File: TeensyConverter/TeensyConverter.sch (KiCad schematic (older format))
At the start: 5 parts, among them P1 CONN_01X03, U1 Teensy-3.2

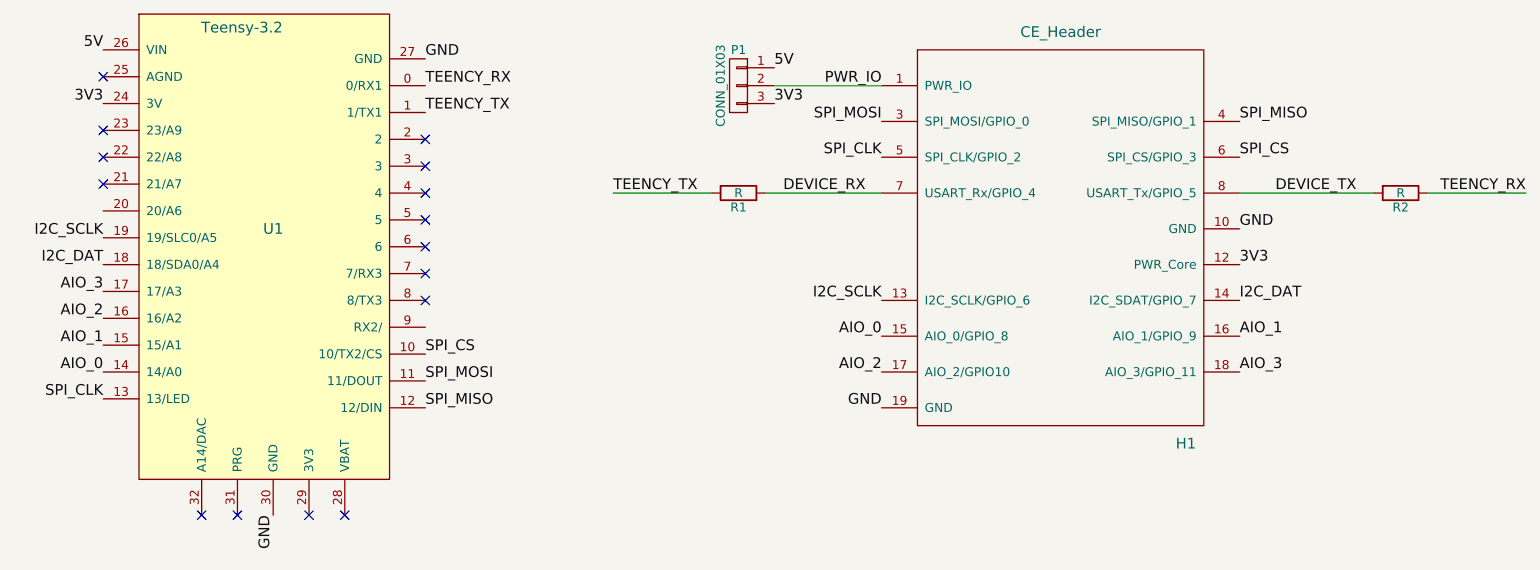
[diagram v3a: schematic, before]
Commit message: Correction to the teensy adapter for the pull ups
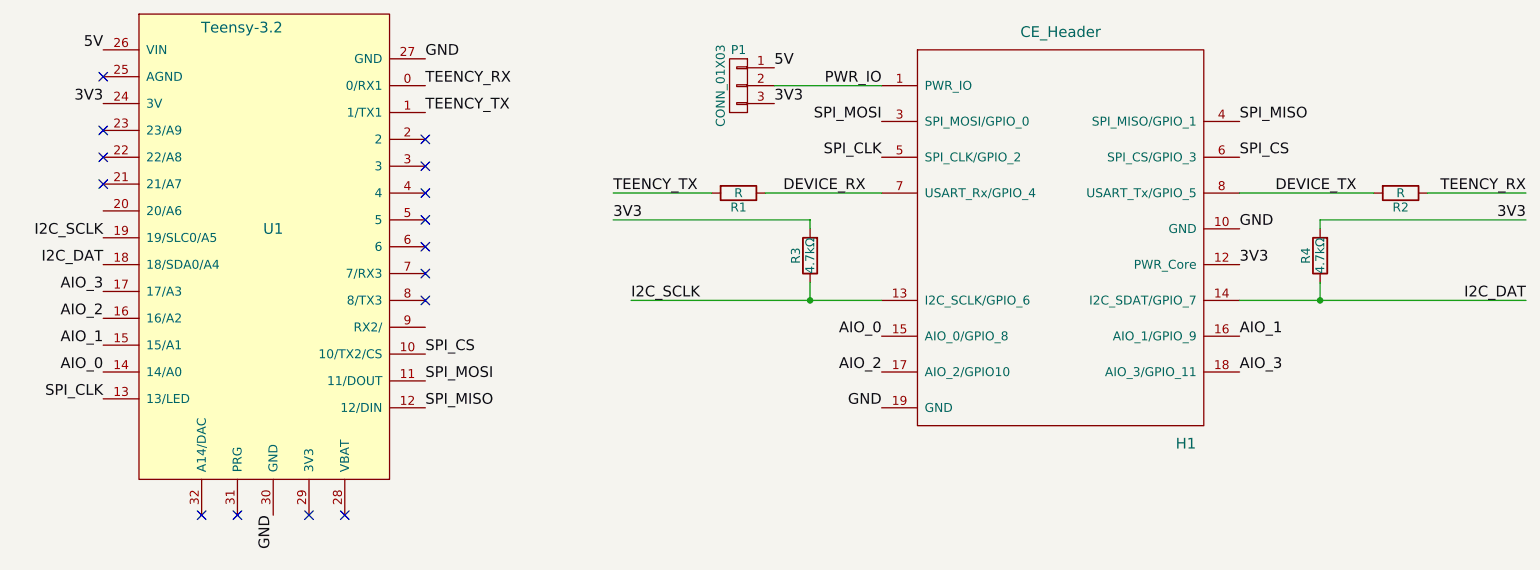
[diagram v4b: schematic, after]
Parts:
- added R3, R4: 4.7kΩ, Resistors_SMD:R_0805_HandSoldering, symbol R
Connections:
- net 3V3: now also R3.2, R4.2
- net I2C_DAT: now also R4.1
- net I2C_SCLK: now also R3.1
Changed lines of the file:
@@
 	-1   0    0    -1
 $EndComp
-Wire Wire Line
-	6550 2500 5950 2500
 Text Label 8550 3500 0    60   ~ 0
 3V3
@@
 	0    1    1    0
 $EndComp
-Wire Wire Line
-	6550 3100 5900 3100
-Wire Wire Line
-	8550 3100 9300 3100
 Text Label 8750 3100 0    60   ~ 0
 DEVICE_TX
@@
 Text Label 4000 2500 0    60   ~ 0
 TEENCY_RX
-Text Label 6550 3700 2    60   ~ 0
-I2C_SCLK
 Text Label 2200 3350 2    60   ~ 0
 I2C_SCLK
-Text Label 8550 3700 0    60   ~ 0
-I2C_DAT
 Text Label 2200 3500 2    60   ~ 0
 I2C_DAT
@@
 Text Label 8550 4100 0    60   ~ 0
 AIO_3
-Wire Wire Line
-	5600 3100 5050 3100
-Wire Wire Line
-	9600 3100 10150 3100
 NoConn ~ 4000 2800
 NoConn ~ 4000 2950
@@
 Text Label 8550 3300 0    60   ~ 0
 GND
+$Comp
+L R R3
+U 1 1 593430C7
+P 6150 3450
+F 0 "R3" V 6230 3450 50  0000 C CNN
+F 1 "4.7kΩ" V 6150 3450 50  0000 C CNN
+F 2 "Resistors_SMD:R_0805_HandSoldering" V 6080 3450 30  0001 C CNN
+F 3 "" H 6150 3450 30  0000 C CNN
+	1    6150 3450
+	-1   0    0    1
+$EndComp
+Text Label 5150 3700 0    60   ~ 0
+I2C_SCLK
+$Comp
+L R R4
+U 1 1 593431DC
+P 9000 3450
+F 0 "R4" V 9080 3450 50  0000 C CNN
+F 1 "4.7kΩ" V 9000 3450 50  0000 C CNN
+F 2 "Resistors_SMD:R_0805_HandSoldering" V 8930 3450 30  0001 C CNN
+F 3 "" H 9000 3450 30  0000 C CNN
+	1    9000 3450
+	-1   0    0    1
+$EndComp
+Wire Wire Line
+	6550 2500 5950 2500
+Wire Wire Line
+	6550 3100 5900 3100
+Wire Wire Line
+	8550 3100 9300 3100
+Wire Wire Line
+	5600 3100 5050 3100
+Wire Wire Line
+	9600 3100 10150 3100
+Wire Wire Line
+	5150 3700 6550 3700
+Wire Wire Line
+	8550 3700 10150 3700
+Text Label 10150 3700 2    60   ~ 0
+I2C_DAT
+Wire Wire Line
+	6150 3600 6150 3700
+Connection ~ 6150 3700
+Wire Wire Line
+	9000 3700 9000 3600
+Connection ~ 9000 3700
+Text Label 5050 3250 0    60   ~ 0
+3V3
+Wire Wire Line
+	6150 3300 6150 3250
+Wire Wire Line
+	6150 3250 5050 3250
+Wire Wire Line
+	9000 3300 9000 3250
+Wire Wire Line
+	9000 3250 10150 3250
+Text Label 10150 3250 2    60   ~ 0
+3V3
 $EndSCHEMATC
